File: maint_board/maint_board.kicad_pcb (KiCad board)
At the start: 2 copper layers, 151.1 x 90.1 mm, 96 parts, among them J1 USB_mini_micro_B, J2 4P4C, J3 TC2030-IDC_FB, K1 KEYSW, K10 KEYSW, K11 KEYSW, K12 KEYSW, K13 KEYSW, K15 KEYSW, K16 KEYSW, K17 KEYSW, K18 KEYSW, K19 KEYSW, K2 KEYSW, K20 KEYSW, K29 KEYSW, K3 KEYSW, K30 KEYSW, K31 KEYSW, K4 KEYSW, K5 KEYSW, K6 KEYSW, K8 KEYSW, K9 KEYSW, Q1 Q_NMOS_GSD, SW1 SW_PUSH, U1 ATMEGA32U4, X1 XTAL_GND

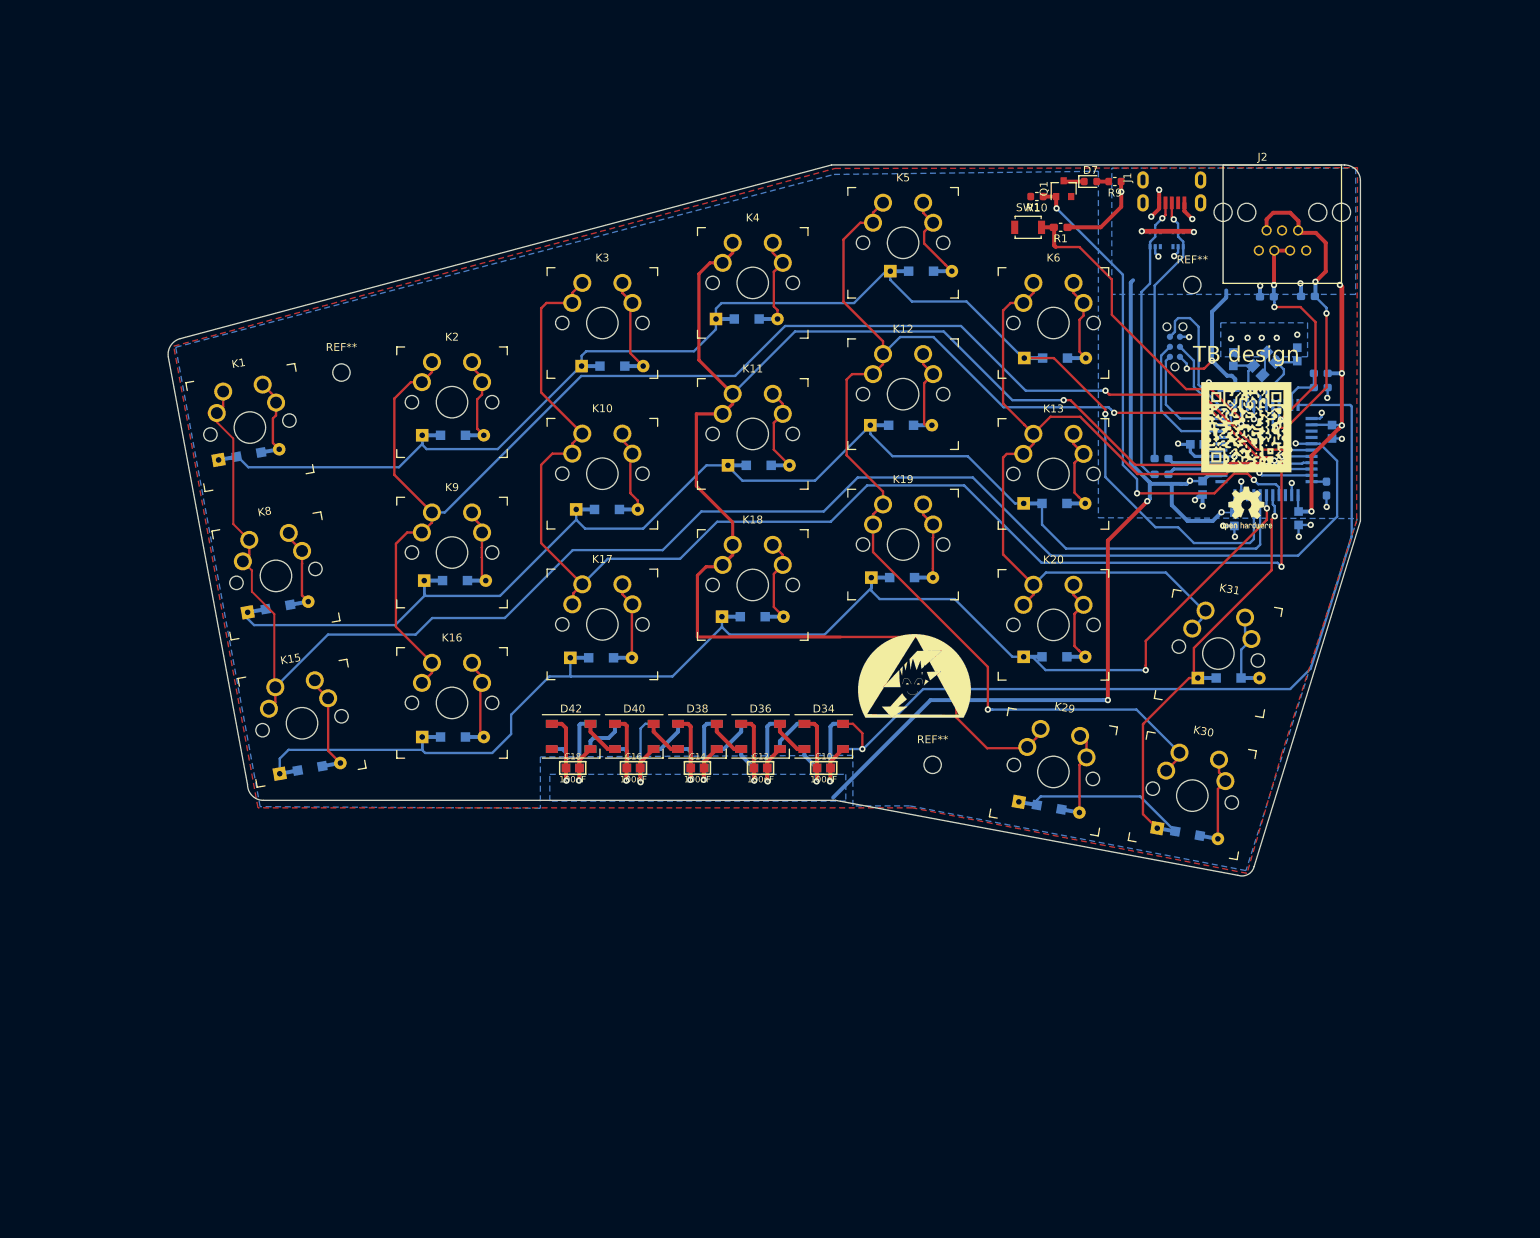
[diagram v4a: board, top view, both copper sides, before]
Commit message: added silk art and cleand upp copper pour
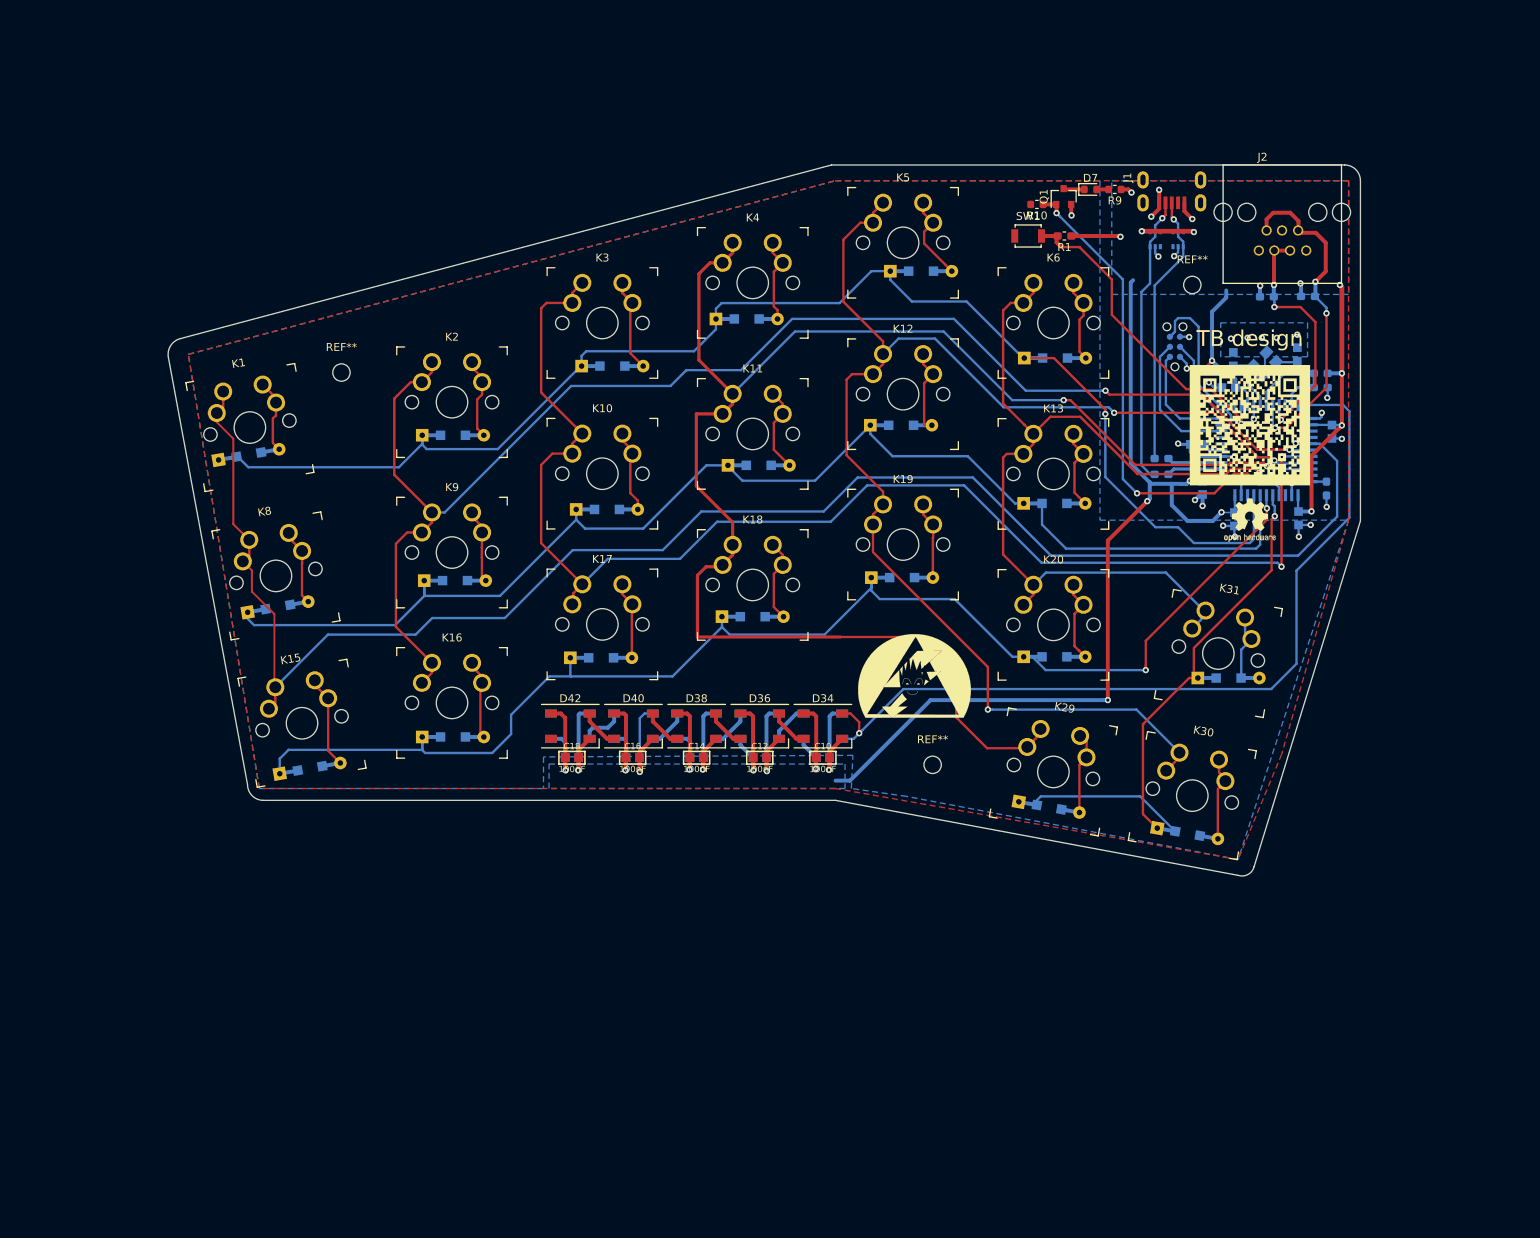
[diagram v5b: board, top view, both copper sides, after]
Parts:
- moved REF** 1.57 mm to (190.5, 74.0)
- moved C15 1.30 mm to (112.3, 104.1)
- moved C16 1.30 mm to (112.3, 104.1)
- moved C17 1.30 mm to (104.6, 104.1)
- moved C18 1.30 mm to (104.6, 104.1)
- moved C10 1.30 mm to (136.4, 104.1)
- moved C11 1.30 mm to (128.4, 104.1)
- moved C12 1.30 mm to (128.4, 104.1)
- moved C13 1.30 mm to (120.4, 104.1)
- moved C14 1.30 mm to (120.4, 104.1)
- moved C9 1.30 mm to (136.4, 104.1)
- moved D33 1.30 mm to (136.4, 100.1)
- moved D34 1.30 mm to (136.4, 100.1)
- moved D35 1.30 mm to (128.4, 100.1)
- moved D36 1.30 mm to (128.4, 100.1)
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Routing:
- net VCC: track 279.4 -> 274.5 mm, vias 22 -> 23
- net /Leds/Din: track 109.3 -> 107.1 mm
- net GND: track 106.6 -> 107.7 mm, vias 30 -> 31
- net Net-(Q1-Pad1): track 64.2 -> 63.1 mm
- net Net-(R1-Pad2): track 42.2 -> 41.1 mm
- net /keys/Col2: track 178.6 -> 179.3 mm
